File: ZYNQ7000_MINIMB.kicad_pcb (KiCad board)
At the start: 4 copper layers, 86 x 69 mm, 154 parts, among them J1 Conn_02x50_Odd_Even, J10 Conn_02x20_Odd_Even, J11 USB_A_Stacked, J12 Conn_01x30, J2 Conn_02x50_Odd_Even, J3 ZYNQ_JTAG, J5 USB_C_Receptacle_USB2.0, J6 HDMI_A, J8 USB_A_Stacked, J9 USB_C_Receptacle_USB2.0, SW2 SW_DIP_x01, SW5 SW_DIP_x02, U1 HR911130A, U2 CP2102N-A01-GQFN28, U4 TXS02612RTWR, U5 TF_Card, U6 TXS0108EPWR, U7 USB3320, U8 TPS2051BDBV, U9 GL850G, Y1 24Mhz, Y2 12Mhz

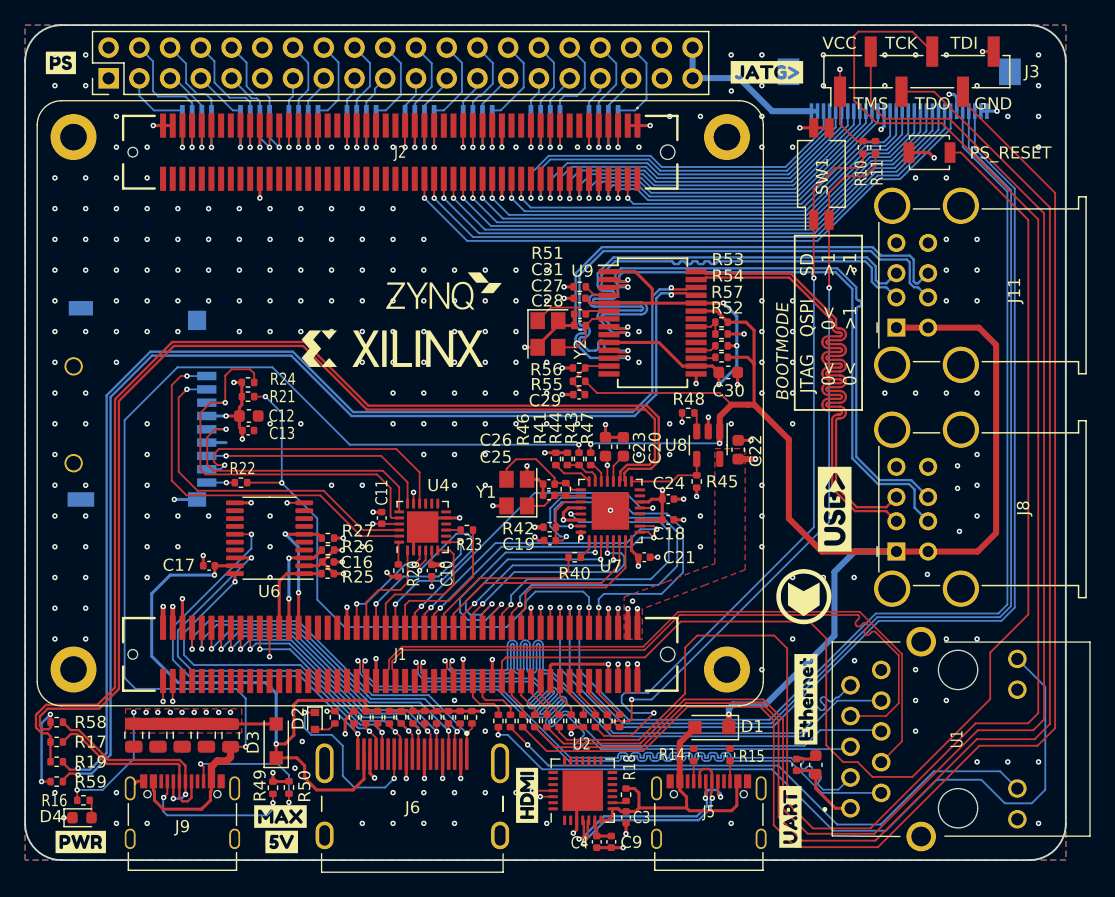
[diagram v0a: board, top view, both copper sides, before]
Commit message: Finall version --fix USB bug
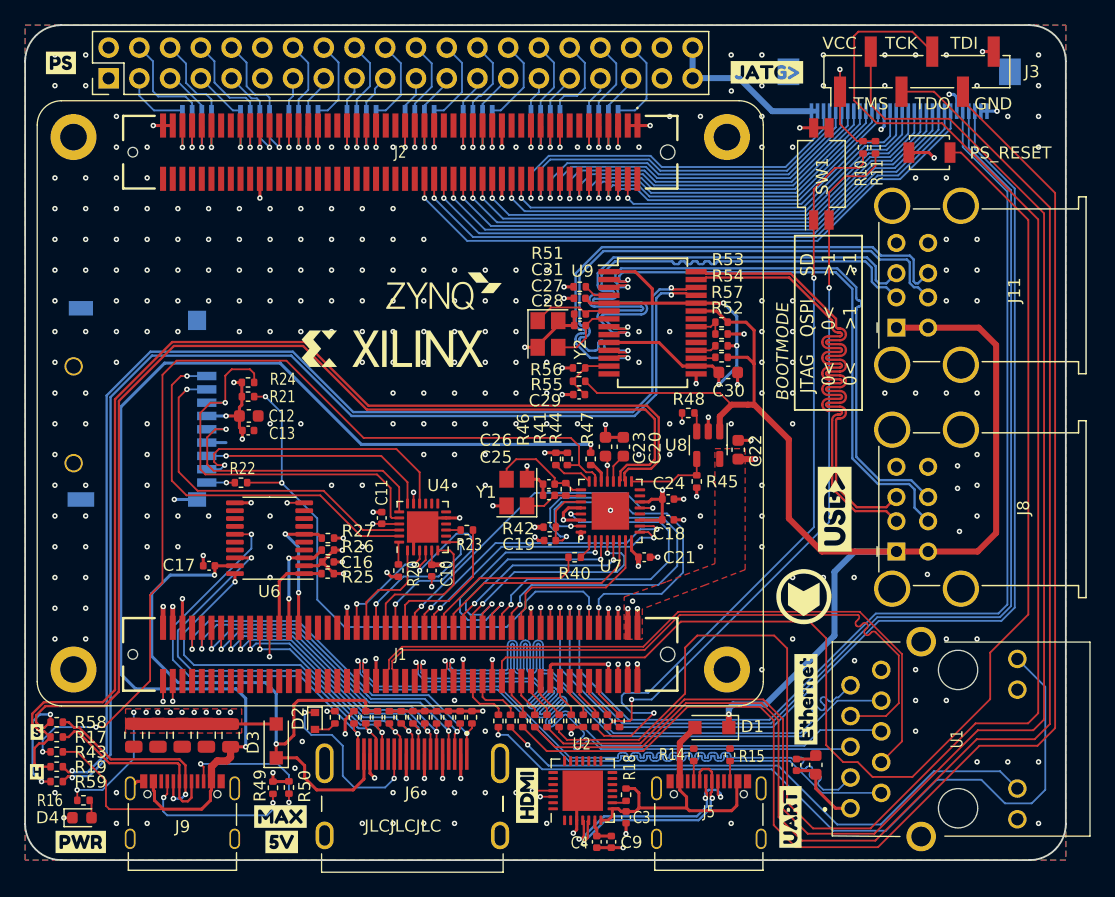
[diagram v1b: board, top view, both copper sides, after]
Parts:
- added kibuzzard-64C3F3C7: G***, kibuzzard-64C3F3C7, F.Cu at (71.0, 112.7)
- added kibuzzard-64C3F3D1: G***, kibuzzard-64C3F3D1, F.Cu at (71.0, 109.4)
- moved R43 49.5 mm to (72.6, 111.1), turned to 0 degrees
- moved R19 0.41 mm to (72.6, 112.3)
- moved R17 0.41 mm to (72.6, 109.8)
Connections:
- R47 pad 1: /USB_5V -> /usb/USB5VIN
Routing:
- net /usb/USB_ID: track 3.16 -> 80.8 mm, vias 0 -> 2
- net /usb/USB5VIN: track 92.0 -> 105.8 mm
- net /USB_5V: track 121.5 -> 109.1 mm, vias 3 -> 1
- net /usb/USB_DP: track 93.0 -> 95.9 mm
- net /usb/USB_DN: track 96.9 -> 98.3 mm
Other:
- board text added: "JLCJLCJLC"
